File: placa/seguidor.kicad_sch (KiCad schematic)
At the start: 18 parts, among them J1 conn_bat, J2 conn_sensores, J3 conn_motor, J4 conn_pwm, SW2 btn_arranque, U1 ATmega328P-P, U2 LM7805_TO220, Y1 Crystal

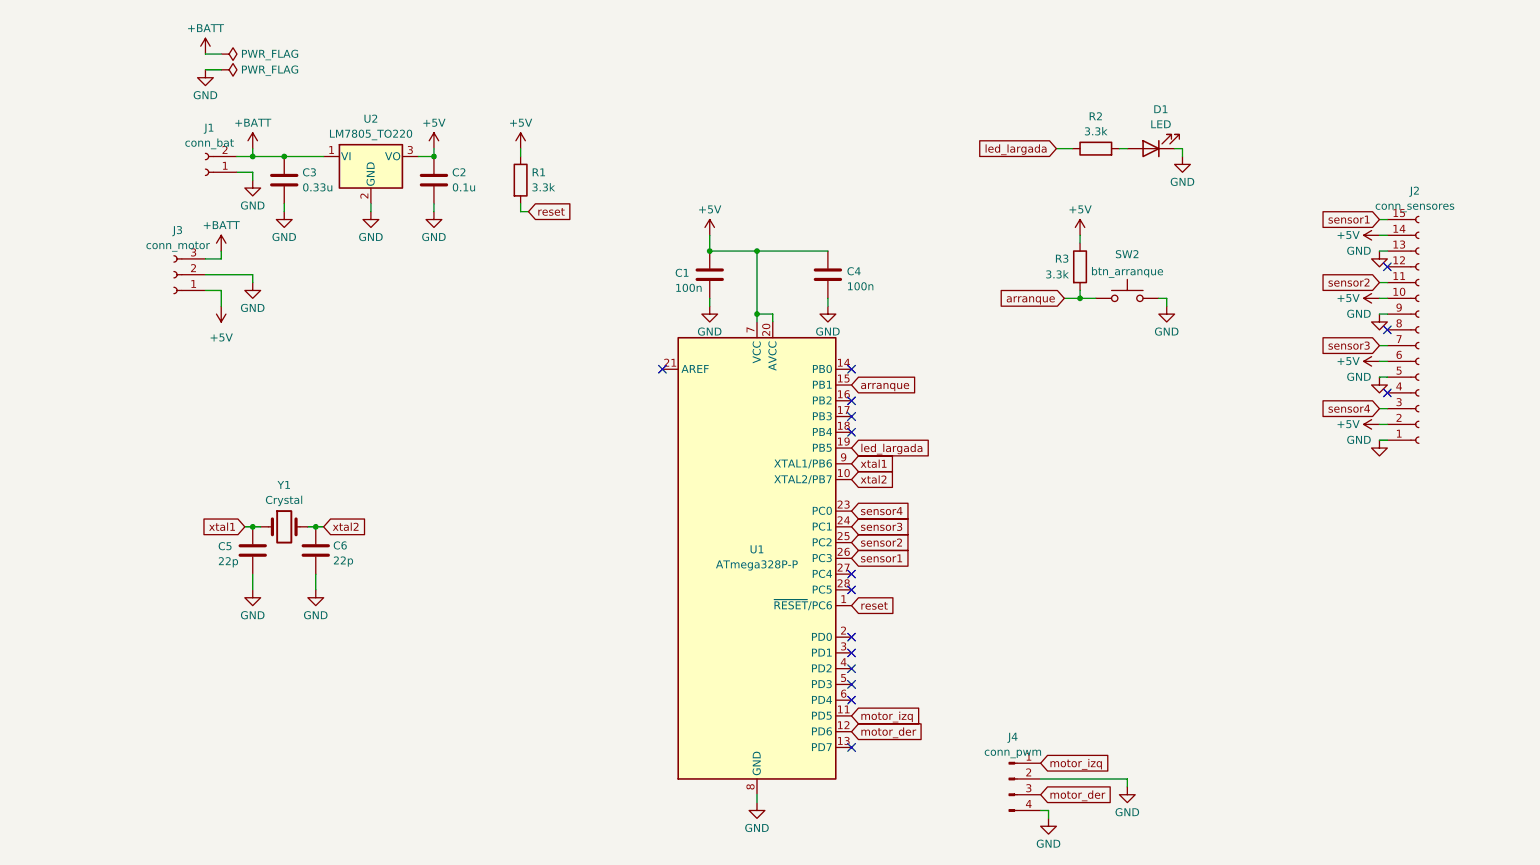
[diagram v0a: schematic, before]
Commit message: placa: agrego conector ICSP, protección de alimentación, botón de reset
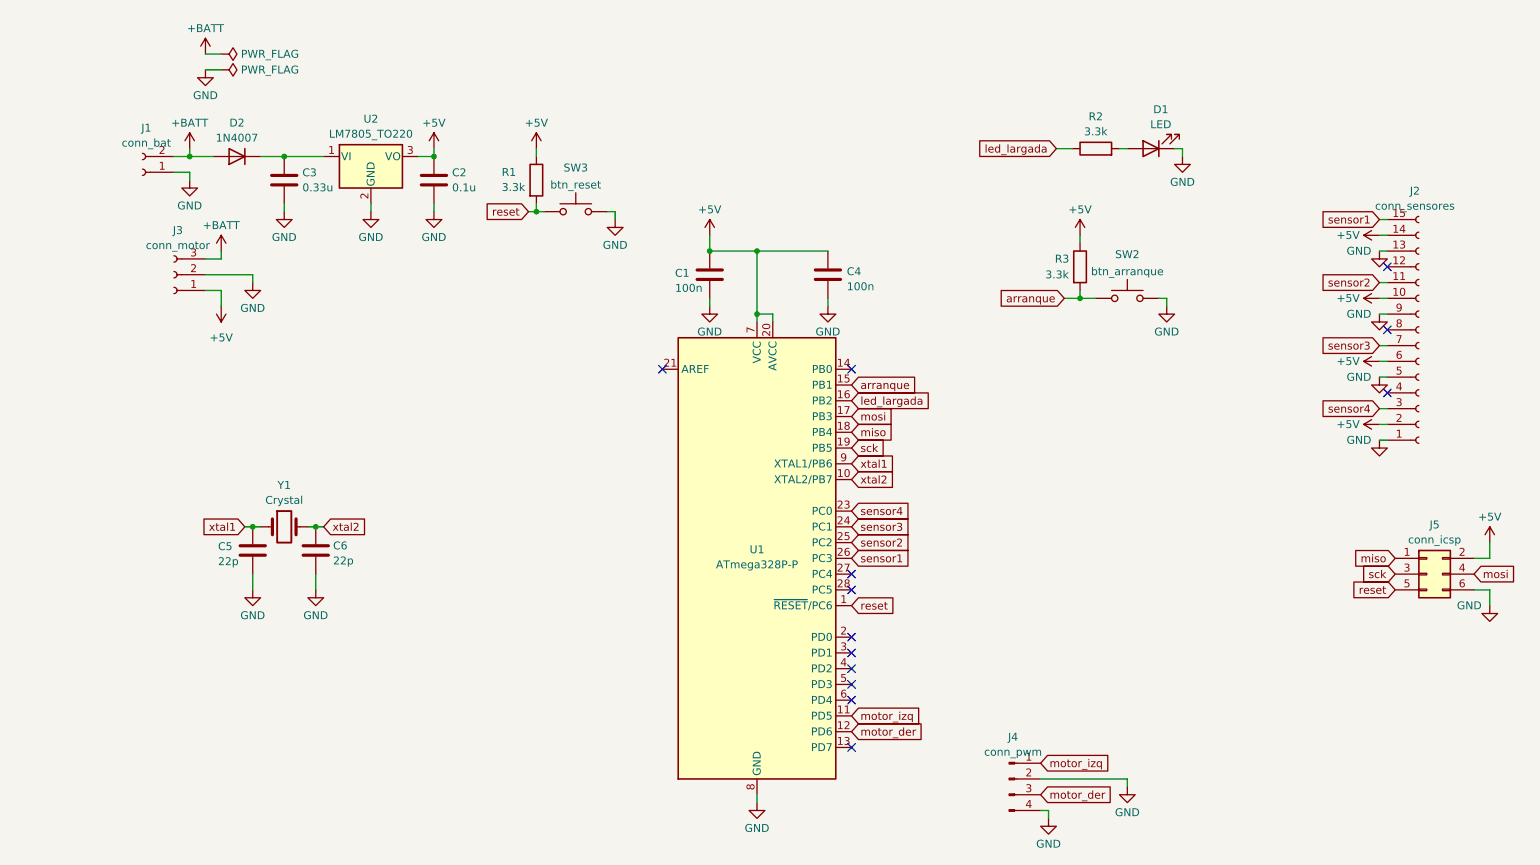
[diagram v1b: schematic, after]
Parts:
- added D2: 1N4007, Diode_THT:D_DO-41_SOD81_P10.16mm_Horizontal, symbol Diode:1N4007
- added J5: conn_icsp, Connector_PinHeader_2.54mm:PinHeader_2x03_P2.54mm_Vertical, symbol Connector_Generic:Conn_02x03_Odd_Even
- added SW3: btn_reset, Button_Switch_THT:SW_PUSH_6mm_H5mm, symbol Switch:SW_Push
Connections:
- net +5V: now also J5.2 (Pin_2)
- net +BATT: now also D2.2 (A); no longer C3.1, U2.1 (VI)
- net GND: now also J5.6 (Pin_6), SW3.2
- net led_largada: now also U1.16 (PB2); no longer U1.19 (PB5)
- net reset: now also J5.5 (Pin_5), SW3.1
- net mosi: now reaches U1.17 (PB3)
- net mosi: now also J5.4 (Pin_4)
- net miso: now reaches U1.18 (PB4)
- net miso: now also J5.1 (Pin_1)
- new net: C3.1, D2.1 (K), U2.1 (VI)
- new net sck: J5.3 (Pin_3), U1.19 (PB5)
- no-connect marks 16 -> 13
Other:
- moved on the sheet: J1, R1

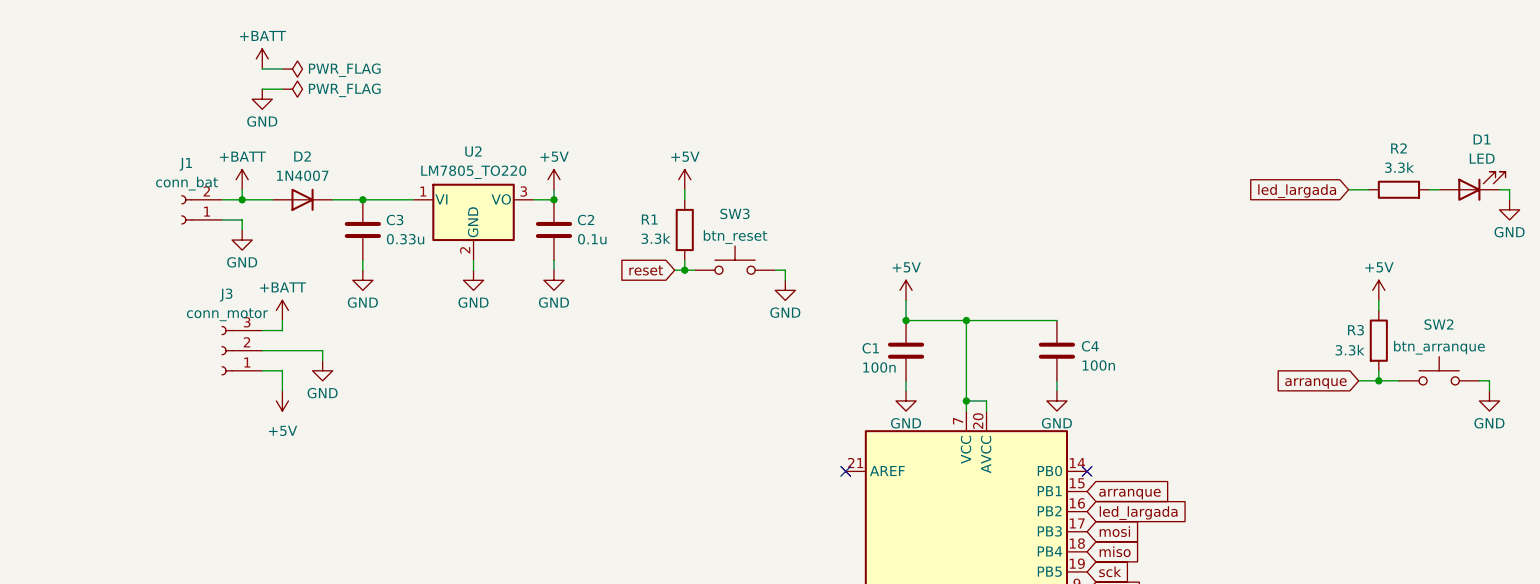
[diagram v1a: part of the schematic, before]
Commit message: placa reordenada y conector spi
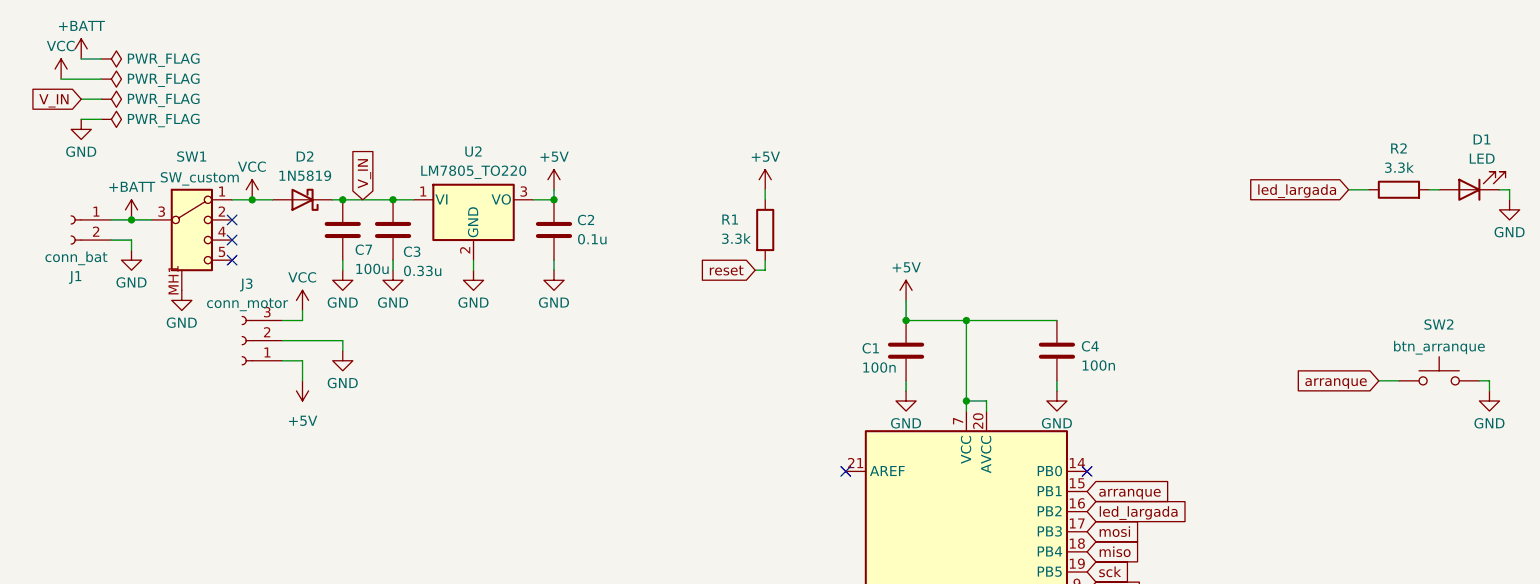
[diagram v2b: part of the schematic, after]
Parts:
- removed D2: 1N4007, Diode_THT:D_DO-41_SOD81_P10.16mm_Horizontal, symbol Diode:1N4007
- removed R3: 3.3k, Resistor_THT:R_Axial_DIN0204_L3.6mm_D1.6mm_P5.08mm_Horizontal, symbol Device:R
- removed SW3: btn_reset, Button_Switch_THT:SW_PUSH_6mm_H5mm, symbol Switch:SW_Push
- added C7: 100u, Capacitor_THT:CP_Radial_D5.0mm_P2.00mm, symbol Device:C
- added D2: 1N5819, Diode_THT:D_DO-41_SOD81_P10.16mm_Horizontal, symbol Diode:1N5819
- added SW1: SW_custom, Custom:Switch custom, symbol custom:SW_custom
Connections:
- net +BATT: now also J1.1 (Pin_1), SW1.3; no longer J1.2 (Pin_2), J3.3 (Pin_3)
- net GND: now also J1.2 (Pin_2), C7.2, SW1.MH1 (CHASIS), SW1.MH2 (CHASIS); no longer J1.1 (Pin_1)
- net V_IN: now reaches C3.1, U2.1 (VI)
- net V_IN: now also C7.1, D2.1 (K)
- new net VCC: D2.2 (A), J3.3 (Pin_3), SW1.1
- no-connect marks 13 -> 16
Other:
- moved on the sheet: C3, J1, J3, R1

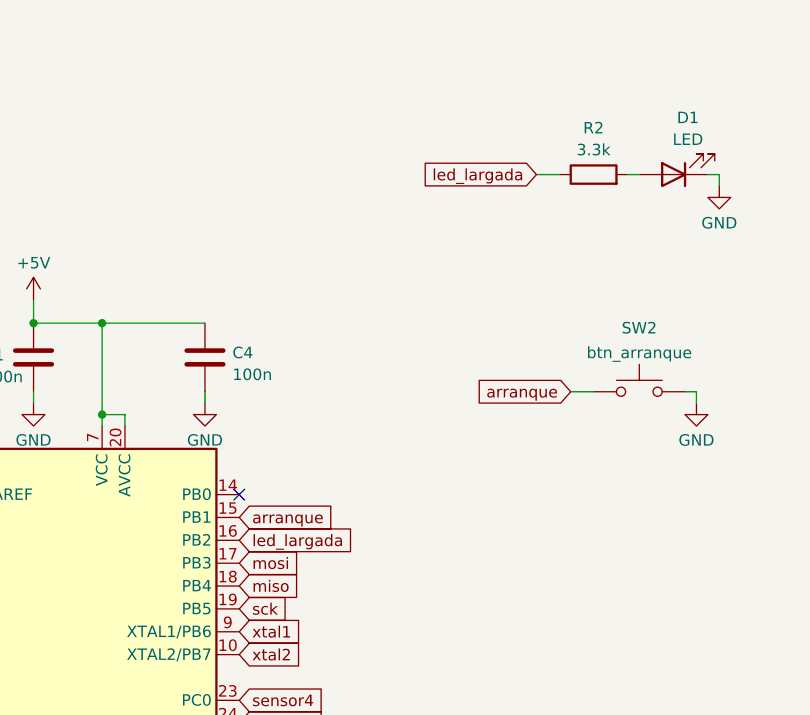
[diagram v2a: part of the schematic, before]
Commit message: pins cambiados. PID ajustado. mensajes de debug.
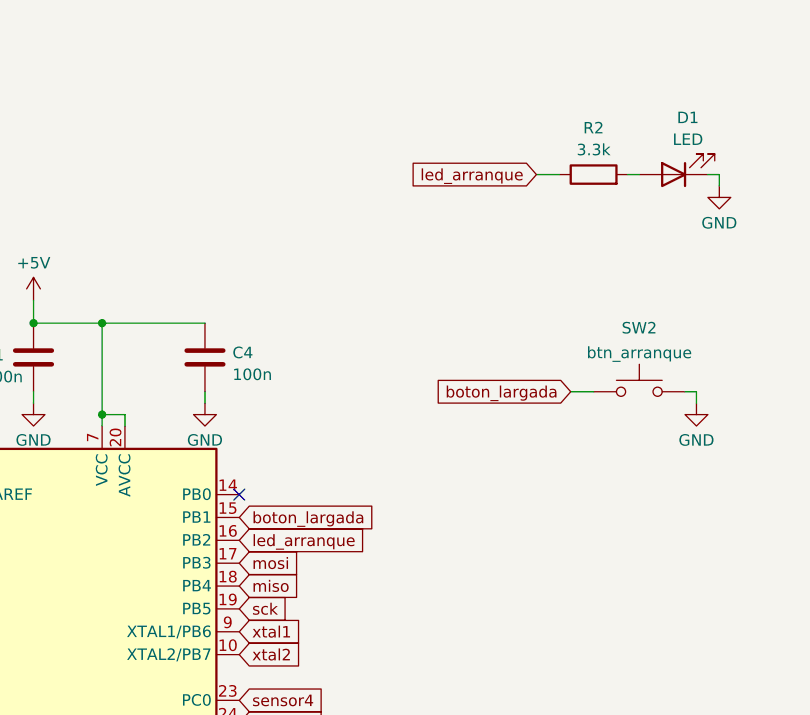
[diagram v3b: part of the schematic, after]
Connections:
- net arranque renamed boton_largada
- net led_largada renamed led_arranque
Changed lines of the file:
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@@
 		)
 	)
-	(global_label "arranque"
+	(global_label "boton_largada"
 		(shape input)
 		(at 146.05 72.39 0)
@@
 		)
 		(property "Intersheetrefs" "${INTERSHEET_REFS}"
-			(at 157.4412 72.39 0)
+			(at 162.5209 72.39 0)
 			(hide yes)
 			(show_name no)
@@
 		)
 	)
-	(global_label "led_largada"
+	(global_label "led_arranque"
 		(shape input)
 		(at 146.05 74.93 0)
@@
 		)
 		(property "Intersheetrefs" "${INTERSHEET_REFS}"
-			(at 160.102 74.93 0)
+			(at 161.3116 74.93 0)
 			(hide yes)
 			(show_name no)
@@
 		)
 	)
-	(global_label "arranque"
+	(global_label "boton_largada"
 		(shape input)
 		(at 182.88 58.42 180)
@@
 		)
 		(property "Intersheetrefs" "${INTERSHEET_REFS}"
-			(at 171.4888 58.42 0)
+			(at 166.4091 58.42 0)
 			(hide yes)
 			(show_name no)
@@
 		)
 	)
-	(global_label "led_largada"
+	(global_label "led_arranque"
 		(shape input)
 		(at 179.07 34.29 180)
@@
 		)
 		(property "Intersheetrefs" "${INTERSHEET_REFS}"
-			(at 165.018 34.29 0)
-			(hide yes)
-			(show_name no)
+			(at 163.8084 34.29 0)
+			(hide yes)
+			(show_name no)
